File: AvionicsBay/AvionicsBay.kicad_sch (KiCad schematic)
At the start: 1 part

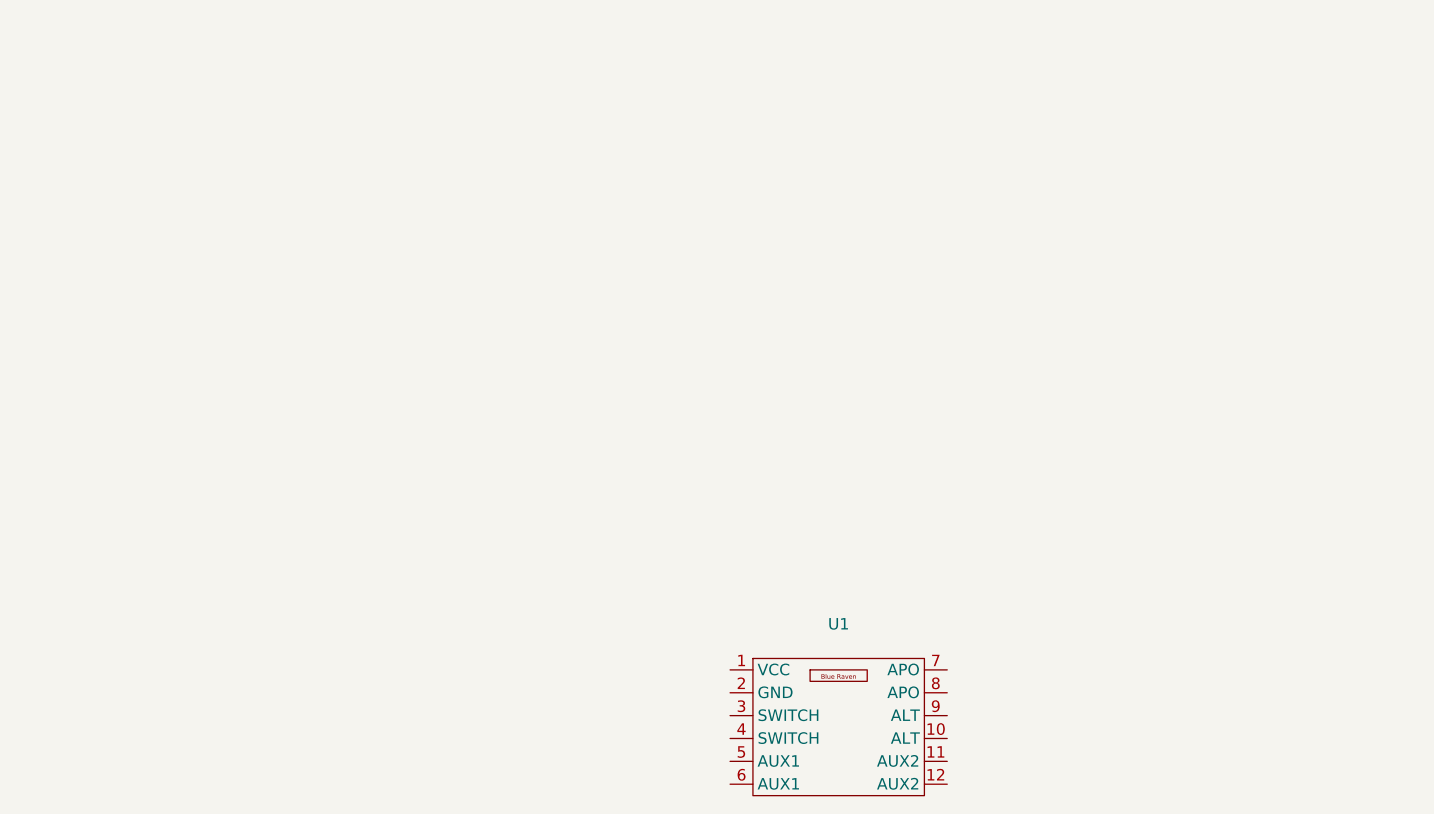
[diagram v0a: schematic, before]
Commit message: Evaluate motors for test flights.
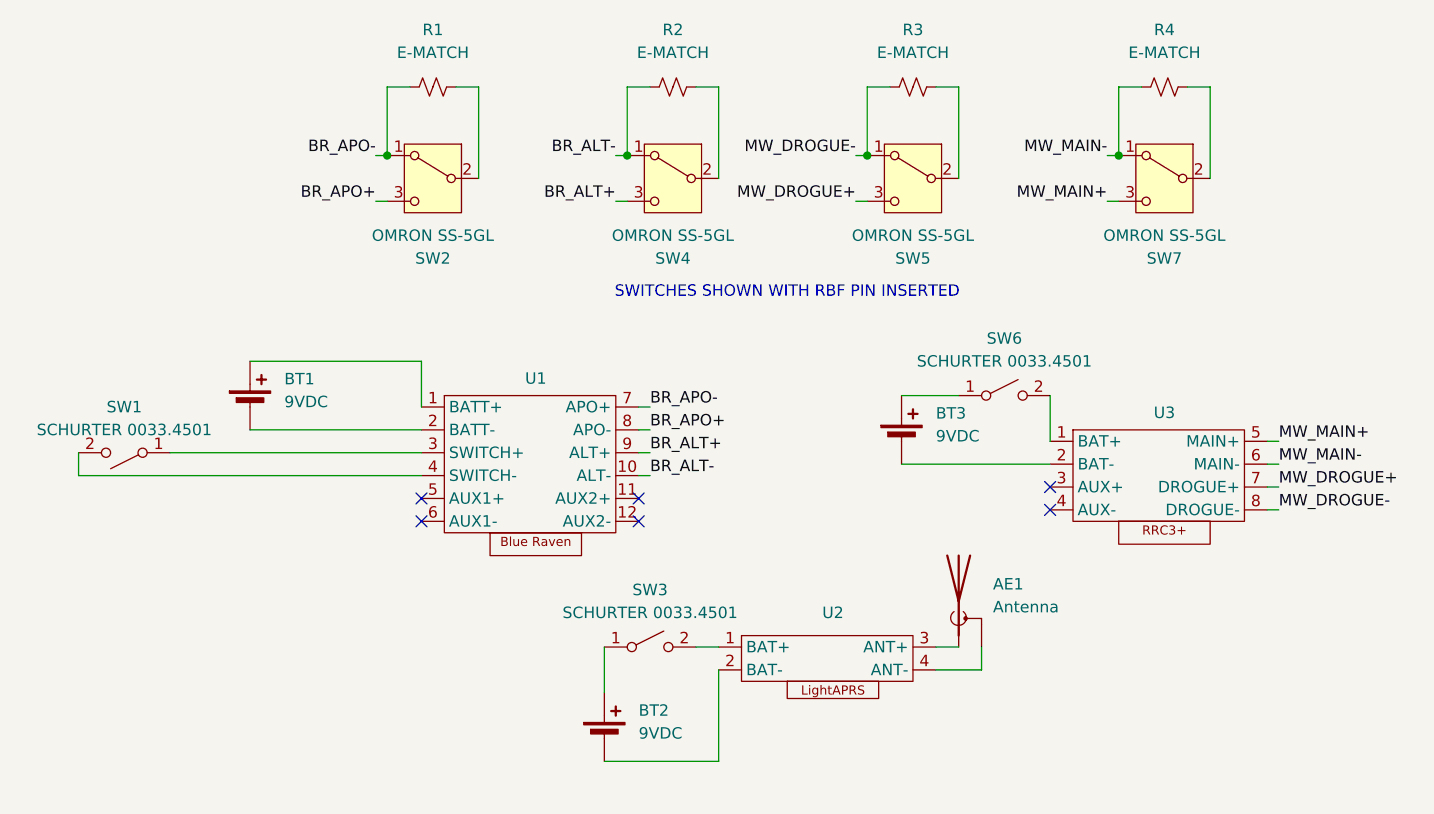
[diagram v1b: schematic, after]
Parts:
- added AE1: Antenna, symbol Device:Antenna_Shield
- added BT1, BT2, BT3: 9VDC, symbol Device:Battery_Cell
- added R1, R2, R3, R4: E-MATCH, symbol Device:R_Small_US
- added SW1, SW3, SW6: SCHURTER 0033.4501, symbol Switch:SW_SPST
- added SW2, SW4, SW5, SW7: OMRON SS-5GL, symbol Switch:SW_SPDT
- added U2: ~, symbol New_Library:LightAPRS
- added U3: ~, symbol New_Library:RRC3+
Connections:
- net at U1.1 (BATT+): now also BT1.1 (+)
- net BR_ALT-: now reaches U1.10 (ALT-)
- net BR_ALT-: now also R2.1, SW4.1 (A)
- net at U1.2 (BATT-): now also BT1.2 (-)
- net at U1.3 (SWITCH+): now also SW1.1 (A)
- net at U1.4 (SWITCH-): now also SW1.2 (B)
- net BR_APO-: now reaches U1.7 (APO+)
- net BR_APO-: now also R1.1, SW2.1 (A)
- net BR_APO+: now reaches U1.8 (APO-)
- net BR_APO+: now also SW2.3 (C)
- net BR_ALT+: now reaches U1.9 (ALT+)
- net BR_ALT+: now also SW4.3 (C)
- new net: R1.2, SW2.2 (B)
- new net: R2.2, SW4.2 (B)
- new net: BT2.1 (+), SW3.1 (A)
- new net: BT2.2 (-), U2.2 (BAT-)
- new net: SW3.2 (B), U2.1 (BAT+)
- new net: R4.2, SW7.2 (B)
- new net: BT3.1 (+), SW6.1 (A)
- new net: SW6.2 (B), U3.1 (BAT+)
- new net: BT3.2 (-), U3.2 (BAT-)
- new net: R3.2, SW5.2 (B)
- new net: AE1.1 (A), U2.3 (ANT+)
- new net: AE1.2 (Shield), U2.4 (ANT-)
- new net MW_DROGUE+: SW5.3 (C), U3.7 (DROGUE+)
- new net MW_DROGUE-: R3.1, SW5.1 (A), U3.8 (DROGUE-)
- new net MW_MAIN+: SW7.3 (C), U3.5 (MAIN+)
- new net MW_MAIN-: R4.1, SW7.1 (A), U3.6 (MAIN-)
- no-connect marks 0 -> 6
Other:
- note added: "SWITCHES SHOWN WITH RBF PIN INSERTED"
- company: (none) -> MIKE MCPHERSON, TRA 27956, NAR 119770 
- title: (none) -> ORCUS AVIONICS
- moved on the sheet: U1
